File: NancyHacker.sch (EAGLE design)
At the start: 7 parts, among them U1 LM3480IM4, U2 ATTINY24QFN

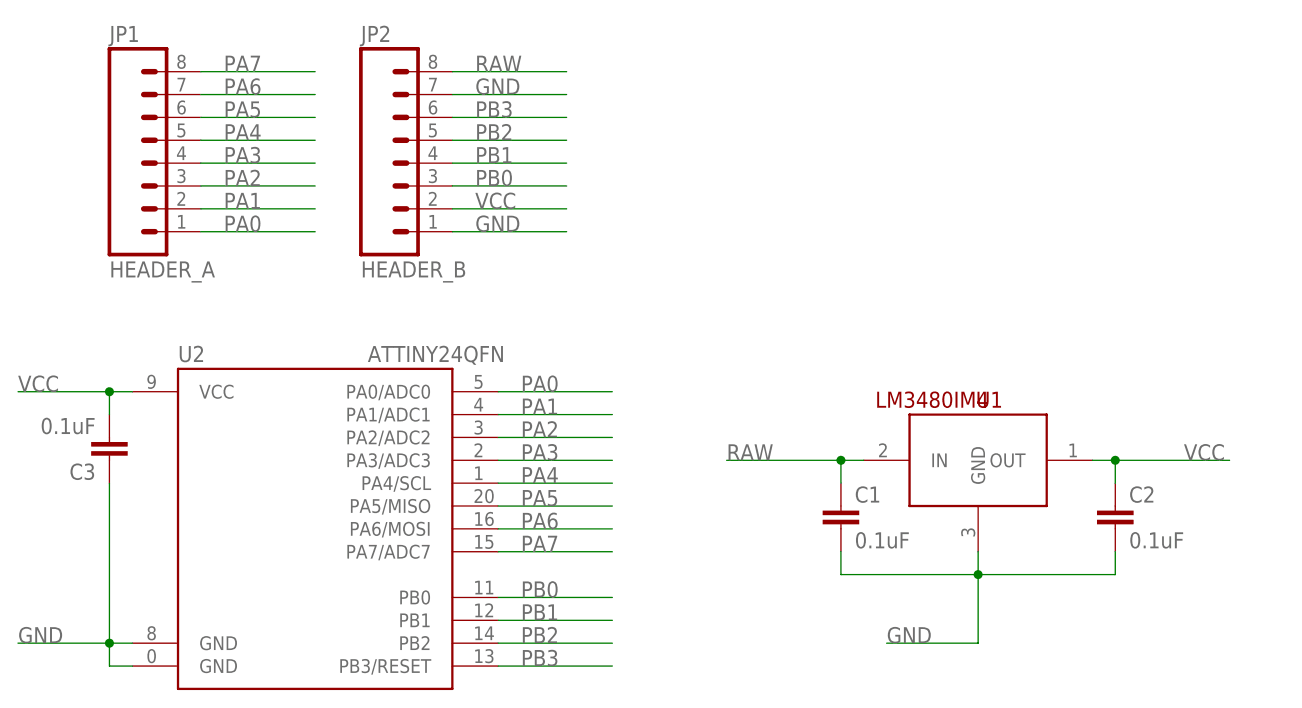
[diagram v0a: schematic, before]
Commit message: Initial commit of forked NancyHacker (Prototype 1)
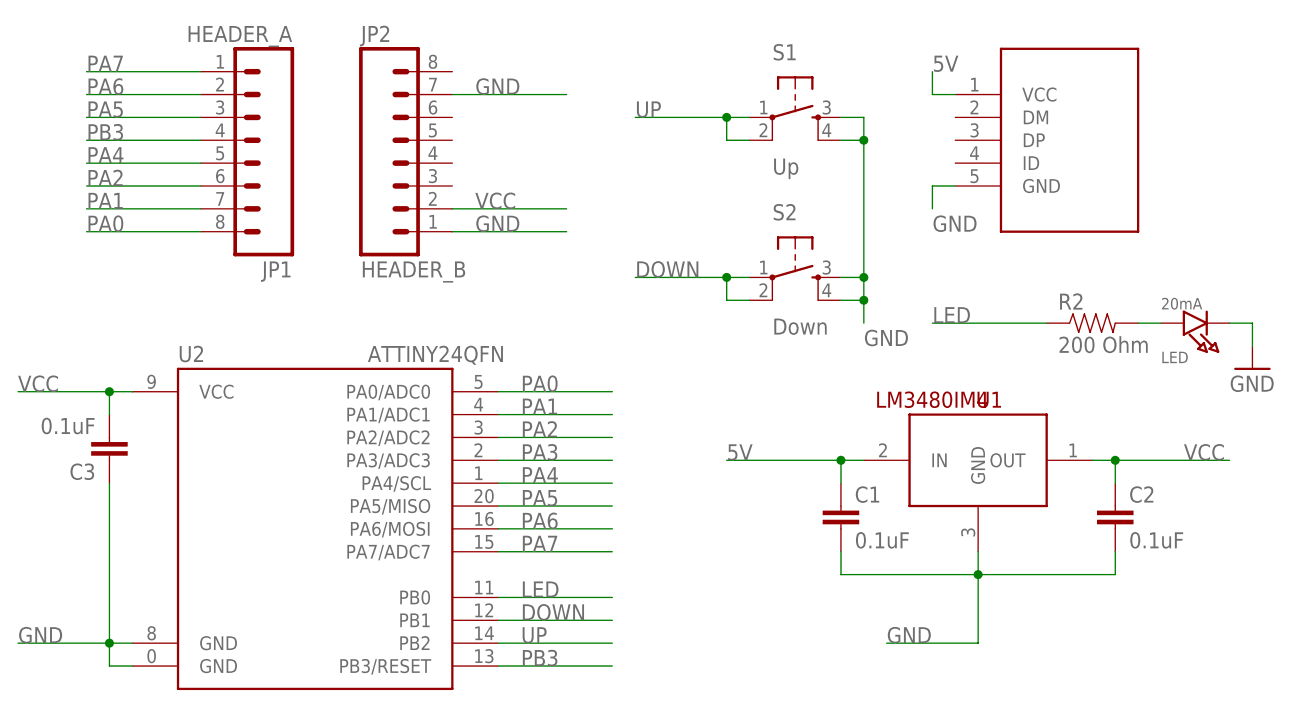
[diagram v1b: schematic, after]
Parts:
- added LED: 20mA, microbuilder:LED0603_NOOUTLINE
- added R2: 200 Ohm, SparkFun-Resistors:RESISTOR0402-RES
- added S1: Up, SparkFun-Electromechanical:TAC_SWITCHSMD
- added S2: Down, SparkFun-Electromechanical:TAC_SWITCHSMD
- added U$1: USB-MICROB-SMDRECEPT, logxen:USB-MICROB-SMDRECEPT
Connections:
- removed net PB0: JP2.3, U2.PB0
- removed net PB1: JP2.4, U2.PB1
- removed net PB2: JP2.5, U2.PB2
- removed net RAW: C1.1, JP2.8, U1.IN
- new net 5V: C1.1, U$1.VCC, U1.IN
- new net DOWN: S2.1, S2.2, U2.PB1
- new net LED: R2.1, U2.PB0
- new net STATUS_LED_RESISTOR: LED.A, R2.2
- new net UP: S1.1, S1.2, U2.PB2
- net GND: now also LED.C, S1.3, S1.4, S2.3, S2.4, U$1.GND
- net PA0: now also JP1.8; no longer JP1.1
- net PA1: now also JP1.7; no longer JP1.2
- net PA2: now also JP1.6; no longer JP1.3
- net PA3: no longer JP1.4
- net PA5: now also JP1.3; no longer JP1.6
- net PA6: now also JP1.2; no longer JP1.7
- net PA7: now also JP1.1; no longer JP1.8
- net PB3: now also JP1.4; no longer JP2.6
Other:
- moved on the sheet: JP1
